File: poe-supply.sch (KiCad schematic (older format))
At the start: 30 parts, among them J3 Barrel_Jack_Switch, U1 MP8007, U2 POE70P-12L

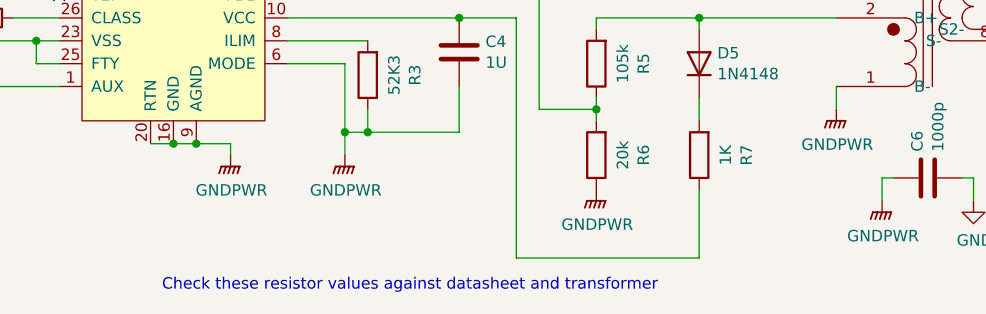
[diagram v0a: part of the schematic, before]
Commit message: Remove note on needing to check POE feedback resistors.
This change also caused kicad to update the cache to use non rescue components
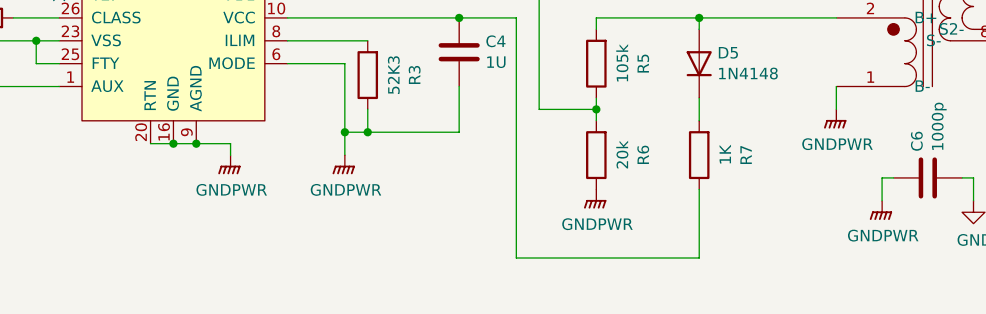
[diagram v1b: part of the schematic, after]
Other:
- note removed: "Check these resistor values against datasheet and transformer"
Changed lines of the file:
@@
 	4800 4000 4600 4000
 Connection ~ 4800 4000
-Text Notes 4050 5700 0    50   ~ 0
-Check these resistor values against datasheet and transformer
 $EndSCHEMATC

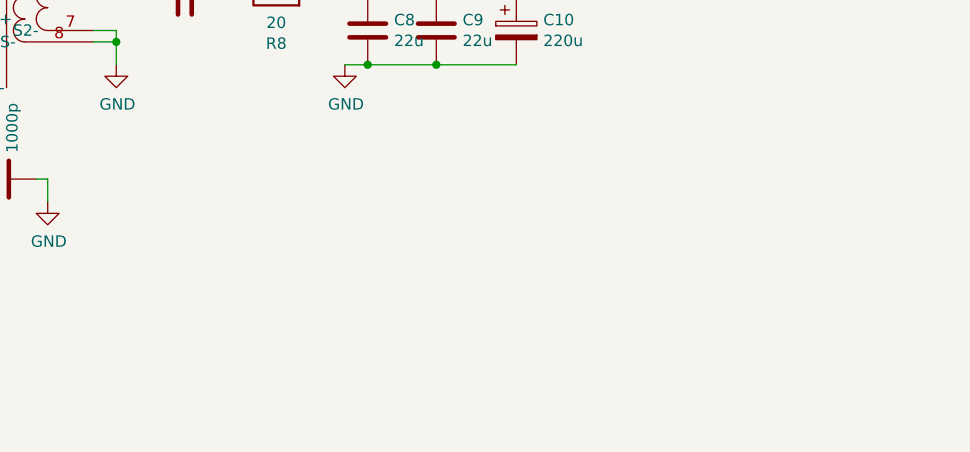
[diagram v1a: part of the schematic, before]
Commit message: Add minor fixes for r1.0 issues
Add load resistors for POE power supply
Add pulldown for buzzer output channel
Mark debug boot resistor as DNP
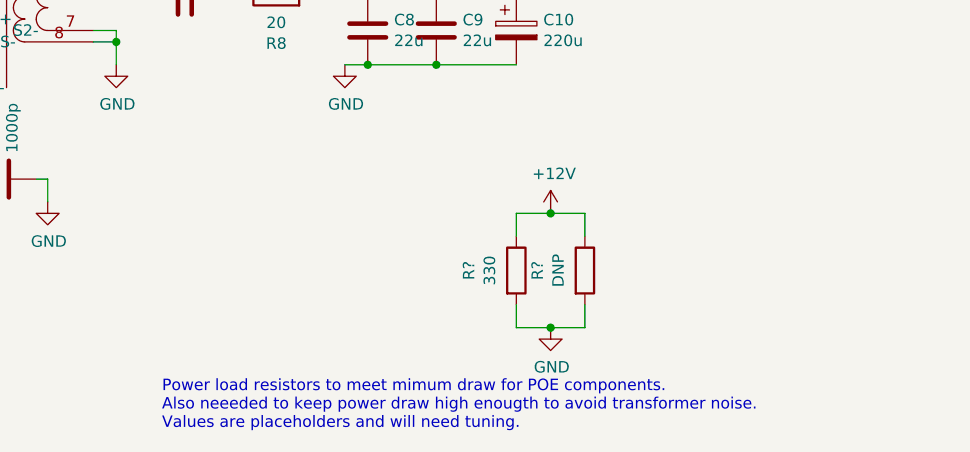
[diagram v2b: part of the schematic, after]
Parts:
- added R?: 330, Resistor_SMD:R_1210_3225Metric, symbol Device:R
- added R?: DNP, Resistor_SMD:R_1210_3225Metric, symbol Device:R
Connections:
- net +12V: now also R?.1, R?.1
- net GND: now also R?.2, R?.2
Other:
- note added: "Power load resistors to meet mimum draw for POE components.\nAlso neeeded to keep power draw high enougth to avoid transformer noise.\nValues are placeholders and will need tuning."
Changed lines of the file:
@@
 	4800 4000 4600 4000
 Connection ~ 4800 4000
+$Comp
+L Device:R R?
+U 1 1 60ABBA44
+P 9650 5600
+F 0 "R?" V 9443 5600 50  0000 C CNN
+F 1 "330" V 9534 5600 50  0000 C CNN
+F 2 "Resistor_SMD:R_1210_3225Metric" V 9580 5600 50  0001 C CNN
+F 3 "~" H 9650 5600 50  0001 C CNN
+	1    9650 5600
+	1    0    0    -1
+$EndComp
+$Comp
+L Device:R R?
+U 1 1 60ABCD5B
+P 9950 5600
+F 0 "R?" V 9743 5600 50  0000 C CNN
+F 1 "DNP" V 9834 5600 50  0000 C CNN
+F 2 "Resistor_SMD:R_1210_3225Metric" V 9880 5600 50  0001 C CNN
+F 3 "~" H 9950 5600 50  0001 C CNN
+	1    9950 5600
+	1    0    0    -1
+$EndComp
+Wire Wire Line
+	9650 5350 9650 5450
+Wire Wire Line
+	9650 5350 9800 5350
+Wire Wire Line
+	9950 5350 9950 5450
+Wire Wire Line
+	9650 5750 9650 5850
+Wire Wire Line
+	9950 5750 9950 5850
+Wire Wire Line
+	9950 5850 9800 5850
+Text Notes 8100 6300 0    50   ~ 0
+Power load resistors to meet mimum draw for POE components.\nAlso neeeded to keep power draw high enougth to avoid transformer noise.\nValues are placeholders and will need tuning.
+$Comp
+L power:+12V #PWR?
+U 1 1 60AE6DBE
+P 9800 5350
+F 0 "#PWR?" H 9800 5200 50  0001 C CNN
+F 1 "+12V" H 9815 5523 50  0000 C CNN
+F 2 "" H 9800 5350 50  0001 C CNN
+F 3 "" H 9800 5350 50  0001 C CNN
+	1    9800 5350
+	1    0    0    -1
+$EndComp
+Connection ~ 9800 5350
+Wire Wire Line
+	9800 5350 9950 5350
+$Comp
+L power:GND #PWR?
+U 1 1 60AE756C
+P 9800 5850
+F 0 "#PWR?" H 9800 5600 50  0001 C CNN
+F 1 "GND" H 9805 5677 50  0000 C CNN
+F 2 "" H 9800 5850 50  0001 C CNN
+F 3 "" H 9800 5850 50  0001 C CNN
+	1    9800 5850
+	1    0    0    -1
+$EndComp
+Connection ~ 9800 5850
+Wire Wire Line
+	9800 5850 9650 5850
 $EndSCHEMATC

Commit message: Add schematic edits to PCB
Add load resistors for POE power supply
Add pulldown for buzzer output channel
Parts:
- gave numbers to parts that had none: 2
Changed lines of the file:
@@
 Connection ~ 4800 4000
 $Comp
-L Device:R R?
+L Device:R R18
 U 1 1 60ABBA44
 P 9650 5600
-F 0 "R?" V 9443 5600 50  0000 C CNN
+F 0 "R18" V 9443 5600 50  0000 C CNN
 F 1 "330" V 9534 5600 50  0000 C CNN
 F 2 "Resistor_SMD:R_1210_3225Metric" V 9580 5600 50  0001 C CNN
@@
 $EndComp
 $Comp
-L Device:R R?
+L Device:R R19
 U 1 1 60ABCD5B
 P 9950 5600
-F 0 "R?" V 9743 5600 50  0000 C CNN
+F 0 "R19" V 9743 5600 50  0000 C CNN
 F 1 "DNP" V 9834 5600 50  0000 C CNN
 F 2 "Resistor_SMD:R_1210_3225Metric" V 9880 5600 50  0001 C CNN
@@
 Power load resistors to meet mimum draw for POE components.\nAlso neeeded to keep power draw high enougth to avoid transformer noise.\nValues are placeholders and will need tuning.
 $Comp
-L power:+12V #PWR?
+L power:+12V #PWR0147
 U 1 1 60AE6DBE
 P 9800 5350
-F 0 "#PWR?" H 9800 5200 50  0001 C CNN
+F 0 "#PWR0147" H 9800 5200 50  0001 C CNN
 F 1 "+12V" H 9815 5523 50  0000 C CNN
 F 2 "" H 9800 5350 50  0001 C CNN
@@
 	9800 5350 9950 5350
 $Comp
-L power:GND #PWR?
+L power:GND #PWR0151
 U 1 1 60AE756C
 P 9800 5850
-F 0 "#PWR?" H 9800 5600 50  0001 C CNN
+F 0 "#PWR0151" H 9800 5600 50  0001 C CNN
 F 1 "GND" H 9805 5677 50  0000 C CNN
 F 2 "" H 9800 5850 50  0001 C CNN

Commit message: Fix small power supply issues
Update POE class resistor to 62 ohms (class 2)
Increase auxiliary winding limit resistor to 5.1k to comply with device current clamp limit
Add Ground test loop
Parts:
- added TP4: TestPoint, TestPoint:TestPoint_Bridge_Pitch5.08mm_Drill0.7mm, symbol Connector:TestPoint
- R1: value 41R2 -> 62
- R7: value 1K -> 5K1
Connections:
- net GND: now also TP4.1
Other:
- note added: "GND loop tespoint"
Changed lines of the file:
@@
 P 3250 4500
 F 0 "R1" V 3043 4500 50  0000 C CNN
-F 1 "41R2" V 3134 4500 50  0000 C CNN
+F 1 "62" V 3134 4500 50  0000 C CNN
 F 2 "Resistor_SMD:R_0603_1608Metric" V 3180 4500 50  0001 C CNN
 F 3 "~" H 3250 4500 50  0001 C CNN
@@
 P 6400 5100
 F 0 "R7" V 6193 5100 50  0000 C CNN
-F 1 "1K" V 6284 5100 50  0000 C CNN
+F 1 "5K1" V 6284 5100 50  0000 C CNN
 F 2 "Resistor_SMD:R_0603_1608Metric" V 6330 5100 50  0001 C CNN
 F 3 "~" H 6400 5100 50  0001 C CNN
@@
 Wire Wire Line
 	9800 5850 9650 5850
+$Comp
+L Connector:TestPoint TP4
+U 1 1 611B68BB
+P 8900 3350
+F 0 "TP4" H 8958 3468 50  0000 L CNN
+F 1 "TestPoint" H 8958 3377 50  0000 L CNN
+F 2 "TestPoint:TestPoint_Bridge_Pitch5.08mm_Drill0.7mm" H 9100 3350 50  0001 C CNN
+F 3 "~" H 9100 3350 50  0001 C CNN
+	1    8900 3350
+	1    0    0    -1
+$EndComp
+$Comp
+L power:GND #PWR0159
+U 1 1 611B70ED
+P 8900 3350
+F 0 "#PWR0159" H 8900 3100 50  0001 C CNN
+F 1 "GND" H 8905 3177 50  0000 C CNN
+F 2 "" H 8900 3350 50  0001 C CNN
+F 3 "" H 8900 3350 50  0001 C CNN
+	1    8900 3350
+	1    0    0    -1
+$EndComp
+Text Notes 8600 3150 0    50   ~ 0
+GND loop tespoint
 $EndSCHEMATC
